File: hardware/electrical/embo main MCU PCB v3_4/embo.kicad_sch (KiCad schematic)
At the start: 109 parts, among them IC1 OPA2354, IC2 OPA2354, J1 Conn_Coaxial, J10 Conn_01x08, J11 Conn_01x08, J12 Conn_01x08, J13 USB_C_Receptacle_USB2.0_16P, J14 24 V PSU input, J15 Conn_01x08, J16 Conn_01x02, J17 Conn_01x02, J18 Conn_01x02, J19 Conn_01x02, J2 Conn_Coaxial, J20 Conn_01x02, J21 Conn_01x02, J22 Conn_01x02, J23 Conn_01x02, J24 Conn_01x04, J25 Conn_01x04, J26 Conn_01x04, J27 Conn_01x04, J28 Conn_01x04, J29 Conn_01x04, J30 Conn_01x02, J31 Conn_01x02, J32 Conn_01x02, J33 Conn_01x02, J4 Conn_01x03, J6 motor 1, J7 motor 2, J8 5V out, J9 Conn_02x10_Odd_Even, Q1 AO4407A, U1 ESP32-S3-WROOM-1, U2 LM2596S-5, U3 AMS1117-3.3

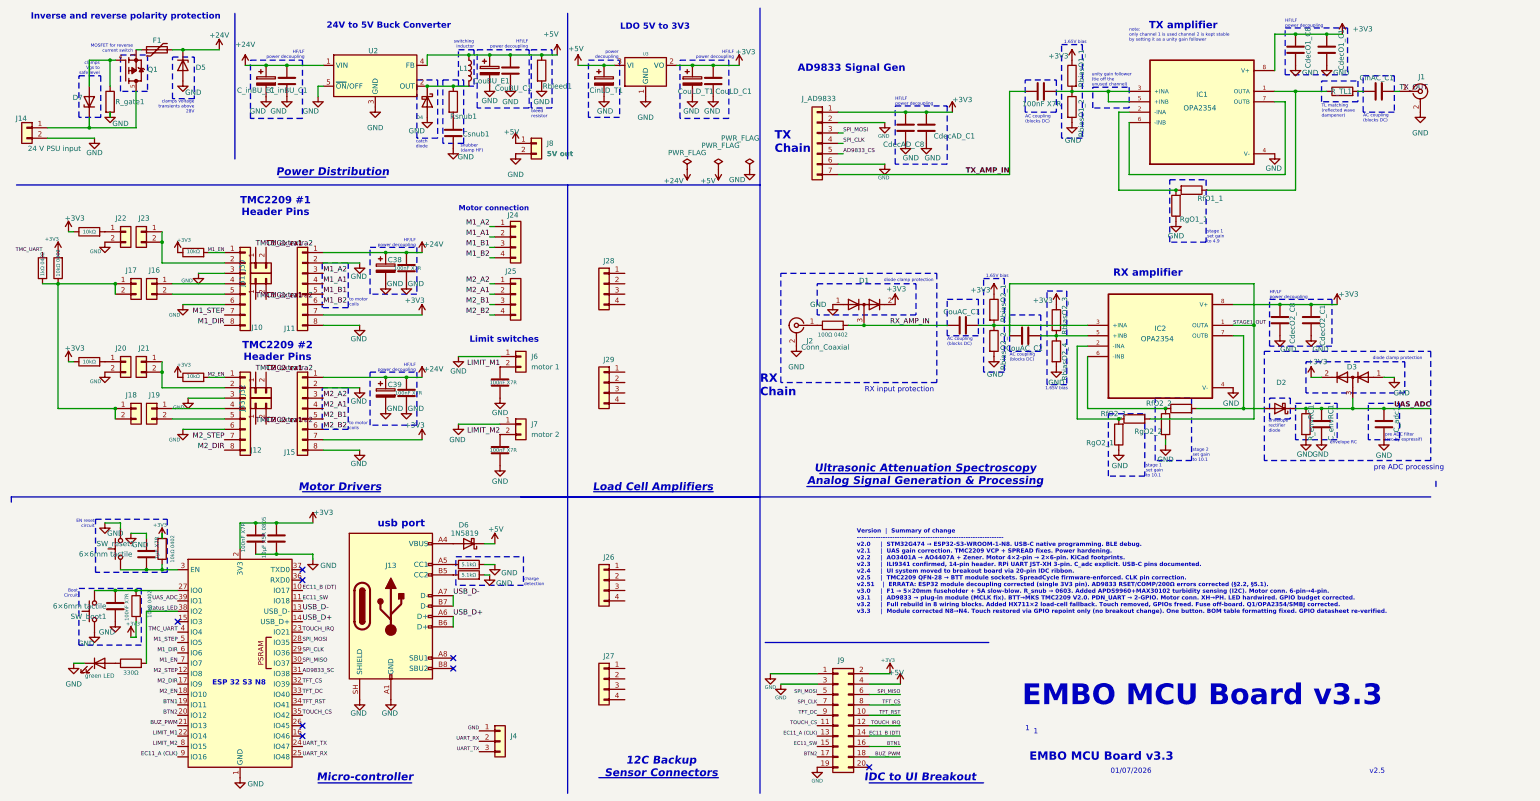
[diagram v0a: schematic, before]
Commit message: MCU PCB v3.4 schematic and routing update
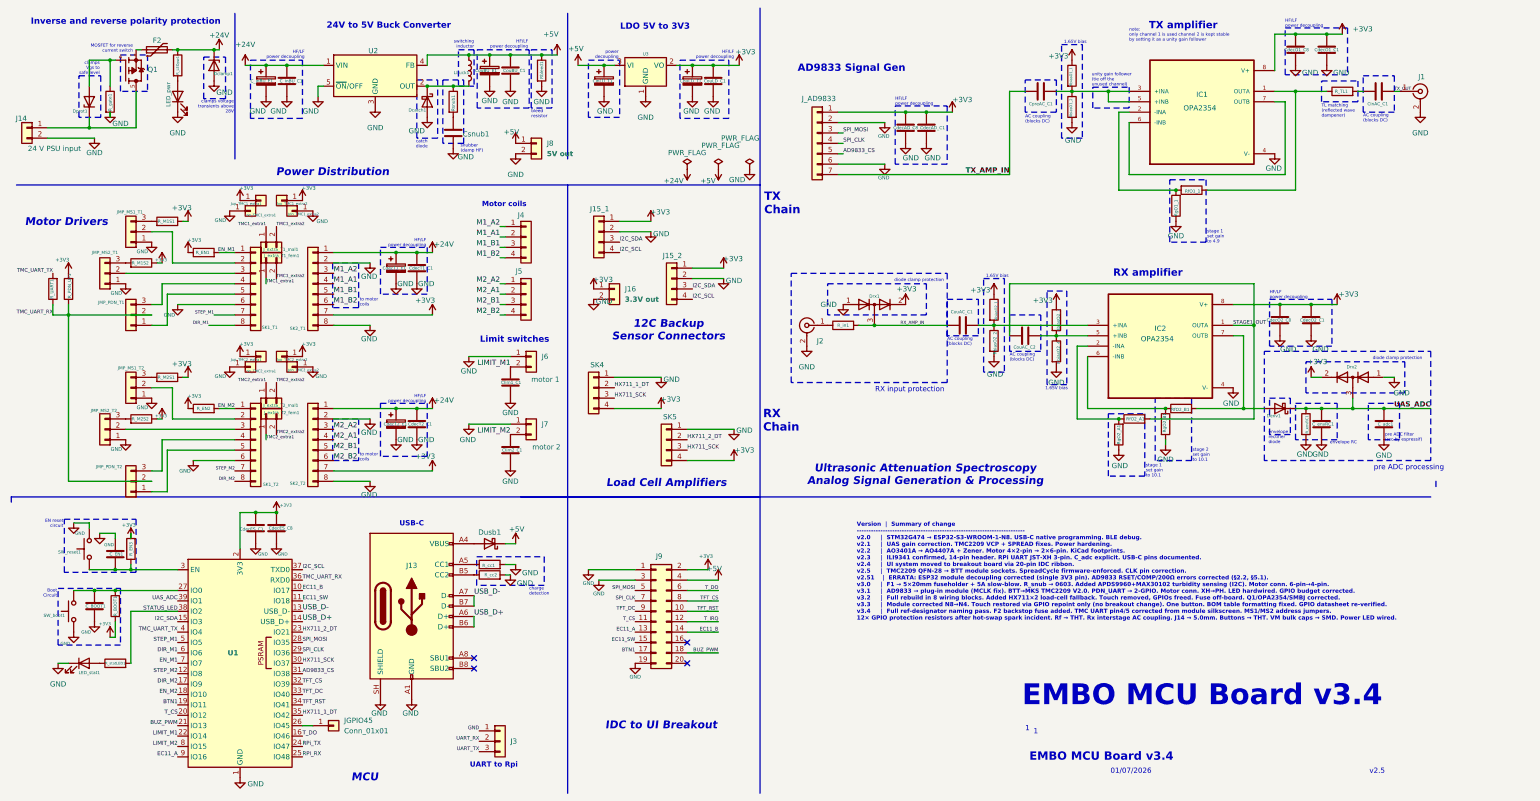
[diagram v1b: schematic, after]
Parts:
- removed J17, J18, J19, J20, J21, J22, J23: Conn_01x02, symbol Connector_Generic:Conn_01x02
- removed R12: 10kΩ, Resistor_SMD:R_0402_1005Metric_Pad0.72x0.64mm_HandSolder, symbol Device:R
- added JGPIO45, Jdo_TMC1_extra1, Jdo_TMC1_extra2, Jdo_TMC2_extra1, Jdo_TMC2_extra2, Jup_TMC1_extra1, Jup_TMC1_extra2, Jup_TMC2_extra1, Jup_TMC2_extra2: Conn_01x01, Connector_PinHeader_2.54mm:PinHeader_1x01_P2.54mm_Vertical, symbol Connector_Generic:Conn_01x01
- added JMP_MS1_T1, JMP_MS1_T2, JMP_MS2_T1, JMP_MS2_T2, JMP_PDN_T1, JMP_PDN_T2: Conn_01x03, Connector_PinHeader_2.54mm:PinHeader_1x03_P2.54mm_Vertical, symbol Connector_Generic:Conn_01x03
- added LED_pwr1: LED_pwr, LED_SMD:LED_0805_2012Metric, symbol Device:LED
- added R_LEDpw1, R_M1S2, R_M2S1, R_M2S2: 10kΩ 0402, Resistor_SMD:R_0402_1005Metric_Pad0.72x0.64mm_HandSolder, symbol Device:R
- CdecT1_E1: renamed from C38; footprint Capacitor_THT:C_Radial_D6.3mm_H7.0mm_P2.50mm -> Capacitor_SMD:CHEMI-HA0
- CdecT2_E1: renamed from C39; footprint Capacitor_THT:C_Radial_D6.3mm_H7.0mm_P2.50mm -> Capacitor_SMD:CHEMI-HA0
- F2: renamed from F1; footprint Fuse:Fuse_1812_4532Metric_Pad1.30x3.40mm_HandSolder -> Fuse:Fuse_2512_6332Metric
- J14: footprint TerminalBlock_Phoenix:TerminalBlock_Phoenix_PT-1,5-2-3.5-H_1x02_P3.50mm_Horizontal -> TerminalBlock_Phoenix:TerminalBlock_Phoenix_MKDS-1,5-2-5.08_1x02_P5.08mm_Horizontal
- J15_1: renamed from J28; footprint (none) -> Connector_JST:JST_XH_B4B-XH-A_1x04_P2.50mm_Vertical
- J15_2: renamed from J29; footprint (none) -> Connector_JST:JST_XH_B4B-XH-A_1x04_P2.50mm_Vertical
- J16: value Conn_01x02 -> 3.3V out; footprint (none) -> Connector_JST:JST_XH_B2B-XH-A_1x02_P2.50mm_Vertical
- J3: renamed from J4; footprint (none) -> Connector_JST:JST_XH_B3B-XH-A_1x03_P2.50mm_Vertical
- J4: renamed from J24; footprint (none) -> Connector_JST:JST_PH_B4B-PH-K_1x04_P2.00mm_Vertical
- J5: renamed from J25; footprint (none) -> Connector_JST:JST_PH_B4B-PH-K_1x04_P2.00mm_Vertical
- J_AD9833: footprint (none) -> Connector_PinSocket_2.54mm:PinSocket_1x07_P2.54mm_Vertical
- J_extra_T1_fem1: renamed from J31; footprint (none) -> Connector_PinSocket_2.54mm:PinSocket_1x02_P2.54mm_Vertical
- J_extra_T1_mal1: renamed from J30; footprint (none) -> Connector_PinHeader_2.54mm:PinHeader_1x02_P2.54mm_Vertical
- J_extra_T2_fem1: renamed from J33; footprint (none) -> Connector_PinSocket_2.54mm:PinSocket_1x02_P2.54mm_Vertical
- J_extra_T2_mal1: renamed from J32; footprint (none) -> Connector_PinHeader_2.54mm:PinHeader_1x02_P2.54mm_Vertical
- R_EN1: renamed from R1; value 10kΩ -> 10kΩ 0402
- R_EN2: renamed from R9; value 10kΩ -> 10kΩ 0402
- R_M1S1: renamed from R13; value 10kΩ -> 10kΩ 0402
- R_gate1: value 10 kΩ 0402 -> 10kΩ 0402
- RbiasO1_1, RbiasO1_2, RbiasO2_1, RbiasO2_2, RbiasO2_3, RbiasO2_4, Rsnub1: value 10kΩ -> 10kΩ 0402
- RfO1_1: footprint Resistor_SMD:R_0402_1005Metric_Pad0.72x0.64mm_HandSolder -> Resistor_THT:R_Axial_DIN0207_L6.3mm_D2.5mm_P10.16mm_Horizontal
- SK4: renamed from J26; footprint (none) -> Connector_PinSocket_2.54mm:PinSocket_1x04_P2.54mm_Vertical
- SK5: renamed from J27; footprint (none) -> Connector_PinSocket_2.54mm:PinSocket_1x04_P2.54mm_Vertical
- SW_boot1, SW_reset1: footprint Button_Switch_SMD:SW_SPST_EVQP2_MiddlePushTravel_H2.5mm -> Button_Switch_THT:SW_PUSH_6mm
- renumbered C41 to C_BOOT1, C10 to C_EN1, C22 to CdecES_C1, C28 to CdecES_C8, C36 to CdecT1_C1, C13 to CdecT2_C1, C17 to Clim1_C1, C18 to Clim2_C1, C35 to CpreAC_C1, D4 to Dcatch1, D5 to Dclamp1, D2 to Denv1, D7 to Dprot1, D1 to Drx1, D3 to Drx2, D6 to Dusb1, L1 to Lbuck1, R41 to R_BOOT1, R40 to R_EN3, R17 to R_cc1, R18 to R_cc2, R6 to R_statLED1, RfO2_1 to RfO2_A1, RfO2_2 to RfO2_B1, RgO2_1 to RgO2_A1, RgO2_2 to RgO2_B1, J10 to SK1_T1, J12 to SK1_T2, J11 to SK2_T1, J15 to SK2_T2
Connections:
- net AD9833_SC is gone; now on net AD9833_CS: U1.31 (IO38)
- net +24V: now also R_LEDpw1.1
- net +3V3: now also J15_1.1 (Pin_1), J15_2.1 (Pin_1), J16.1 (Pin_1), SK4.4 (Pin_4), SK5.4 (Pin_4), Jup_TMC1_extra1.1 (Pin_1), Jup_TMC1_extra2.1 (Pin_1), Jup_TMC2_extra1.1 (Pin_1), Jup_TMC2_extra2.1 (Pin_1), R_M1S2.1, R_M2S1.1, R_M2S2.1
- net BTN1: now also J9.17 (Pin_17); no longer J9.16 (Pin_16)
- net GND: now also J15_1.2 (Pin_2), J15_2.2 (Pin_2), J16.2 (Pin_2), SK4.1 (Pin_1), SK5.1 (Pin_1), JMP_MS1_T1.1 (Pin_1), JMP_MS1_T2.1 (Pin_1), JMP_MS2_T1.1 (Pin_1), JMP_MS2_T2.1 (Pin_1), Jdo_TMC1_extra1.1 (Pin_1), Jdo_TMC1_extra2.1 (Pin_1), Jdo_TMC2_extra1.1 (Pin_1), Jdo_TMC2_extra2.1 (Pin_1), LED_pwr1.1 (K); no longer SK1_T1.3 (Pin_3), SK1_T2.3 (Pin_3)
- net UART_RX: no longer U1.25 (IO48)
- net UART_TX: no longer U1.24 (IO47)
- net at R_M1S1.2: now also JMP_MS1_T1.3 (Pin_3)
- net at SK1_T2.2 (Pin_2): now also JMP_MS1_T2.2 (Pin_2)
- net I2C_SDA: now reaches U1.15 (IO3)
- net I2C_SDA: now also J15_1.3 (Pin_3), J15_2.3 (Pin_3)
- net T_DO: now reaches U1.16 (IO46)
- net T_DO: now also J9.6 (Pin_6)
- net at U1.26 (IO45): now also JGPIO45.1 (Pin_1)
- net TMC_UART_RX: now reaches U1.36 (RXD0)
- net TMC_UART_RX: now also R_PDN_UP1.1, R_UART1.1, JMP_PDN_T1.2 (Pin_2), JMP_PDN_T2.2 (Pin_2)
- net I2C_SCL: now reaches U1.37 (TXD0)
- net I2C_SCL: now also J15_1.4 (Pin_4), J15_2.4 (Pin_4)
- net at SK1_T1.4 (Pin_4): now also JMP_PDN_T1.3 (Pin_3); no longer J16.1 (Pin_1)
- net at SK1_T1.5 (Pin_5): now also JMP_PDN_T1.1 (Pin_1); no longer J16.2 (Pin_2)
- net at SK1_T1.2 (Pin_2): now also JMP_MS1_T1.2 (Pin_2)
- net at SK1_T2.4 (Pin_4): now also JMP_PDN_T2.3 (Pin_3)
- net at SK1_T2.5 (Pin_5): now also JMP_PDN_T2.1 (Pin_1)
- net HX711_1_DT: now reaches SK4.2 (Pin_2)
- net HX711_1_DT: now also U1.35 (IO42)
- net HX711_SCK: now reaches SK4.3 (Pin_3)
- net HX711_SCK: now also SK5.3 (Pin_3), U1.30 (IO37)
- net HX711_2_DT: now reaches SK5.2 (Pin_2)
- net HX711_2_DT: now also U1.23 (IO21)
- net BTN2 renamed T_CS
- net T_CS: now also J9.11 (Pin_11); no longer J9.17 (Pin_17)
- net EC11_A (CLK) renamed EC11_A
- net EC11_B (DT) renamed EC11_B
- net M1_DIR renamed DIR_M1
- net M1_EN renamed EN_M1
- net M1_STEP renamed STEP_M1
- net M2_DIR renamed DIR_M2
- net M2_EN renamed EN_M2
- net M2_STEP renamed STEP_M2
- removed net SPI_MISO: J9.6 (Pin_6), U1.30 (IO37)
- net TMC_UART renamed TMC_UART_TX
- removed net TOUCH_CS: J9.11 (Pin_11), U1.35 (IO42)
- net TOUCH_IRQ renamed T_IRQ
- net T_IRQ: no longer U1.23 (IO21)
- net status_LED renamed STATUS_LED
- new net: JMP_MS2_T1.3 (Pin_3), R_M1S2.2
- new net: JMP_MS1_T2.3 (Pin_3), R_M2S1.2
- new net: JMP_MS2_T1.2 (Pin_2), SK1_T1.3 (Pin_3)
- new net: LED_pwr1.2 (A), R_LEDpw1.2
- new net: JMP_MS2_T2.2 (Pin_2), SK1_T2.3 (Pin_3)
- new net: JMP_MS2_T2.3 (Pin_3), R_M2S2.2
- new net RPi_RX: U1.25 (IO48)
- new net RPi_TX: U1.24 (IO47)
- no-connect marks 8 -> 4
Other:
- note added: "EMBO MCU Board v3.4"
- note added: "MCU"
- note added: "Motor coils"
- note added: "UART to Rpi"
- note added: "USB-C"
- note added: "Version | Summary of change ----------------------------------------------------------------------- v2.0 | STM32G474 → ESP32-S3-WROOM-1-N8. USB-C native programming. BLE debug. v2.1 | UAS gain correction. TMC2209 VCP + SPREAD fixes. Power hardening. v2.2 | AO3401A → AO4407A + Zener. Motor 4×2-pin → 2×6-pin. KiCad footprints. v2.3 | ILI9341 confirmed, 14-pin header. RPi UART JST-XH 3-pin. C_adc ex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"
- note removed: "EMBO MCU Board v3.3"
- note removed: "ESP 32 S3 N8"
- note removed: "Micro-controller"
- note removed: "Motor connection"
- note removed: "TMC2209 #1 Header Pins"
- note removed: "TMC2209 #2 Header Pins"
- note removed: "Version | Summary of change -------------------------------------------------------------- v2.0 | STM32G474 → ESP32-S3-WROOM-1-N8. USB-C native programming. BLE debug. v2.1 | UAS gain correction. TMC2209 VCP + SPREAD fixes. Power hardening. v2.2 | AO3401A → AO4407A + Zener. Motor 4×2-pin → 2×6-pin. KiCad footprints. v2.3 | ILI9341 confirmed, 14-pin header. RPi UART JST-XH 3-pin. C_adc explicit. U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"
- note removed: "usb port"
- moved on the sheet: CdecT1_E1, CdecT2_E1, Dclamp1, Drx1, Dusb1, J13, J15_1, J15_2, J2, J4, J5, J6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

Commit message: finish PCB v3.4 routing
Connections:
- net UART_RX is gone; now on net RPi_RX: J3.2 (Pin_2)
- net UART_TX is gone; now on net RPi_TX: J3.3 (Pin_3)
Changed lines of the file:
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@@
+		)
+	)
+	(label "RPi_RX"
+		(at 125.73 191.77 180)
+		(effects
+			(font
+				(size 0.9652 0.9652)
+				(thickness 0.1207)
+			)
+			(justify right bottom)
 		)
 	)
@@
 		)
 	)
+	(label "RPi_TX"
+		(at 125.73 194.31 180)
+		(effects
+			(font
+				(size 0.9652 0.9652)
+				(thickness 0.1207)
+			)
+			(justify right bottom)
+		)
+	)
 	(label "STEP_M1"
 		(at 60.96 87.63 180)
@@
 		)
 	)
-	(label "UART_RX"
-		(at 125.73 191.77 180)
-		(effects
-			(font
-				(size 0.889 0.889)
-				(thickness 0.1111)
-			)
-			(justify right bottom)
-		)
-	)
 	(label "M1_B1"
 		(at 90.17 82.55 0)
@@
 			)
 			(justify right bottom)
-		)
-	)
-	(label "UART_TX"
-		(at 125.73 194.31 180)
-		(effects
-			(font
-				(size 0.889 0.889)
-				(thickness 0.1111)
-			)
-			(justify right bottom)

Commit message: v3.4 PCb final changes
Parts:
- J4, J5: footprint Connector_JST:JST_PH_B4B-PH-K_1x04_P2.00mm_Vertical -> Connector_JST:JST_XH_B4B-XH-A_1x04_P2.50mm_Vertical
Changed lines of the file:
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@@
 			)
 		)
-		(property "Footprint" "Connector_JST:JST_PH_B4B-PH-K_1x04_P2.00mm_Vertical"
+		(property "Footprint" "Connector_JST:JST_XH_B4B-XH-A_1x04_P2.50mm_Vertical"
 			(at 137.16 82.55 0)
 			(hide yes)
@@
 			)
 		)
-		(property "Footprint" "Connector_JST:JST_PH_B4B-PH-K_1x04_P2.00mm_Vertical"
+		(property "Footprint" "Connector_JST:JST_XH_B4B-XH-A_1x04_P2.50mm_Vertical"
 			(at 137.16 68.58 0)
 			(hide yes)
